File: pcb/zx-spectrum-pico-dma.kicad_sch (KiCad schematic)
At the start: 1 part, among them U101 RP2350_Stamp_XL

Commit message: pull in board from zx diagnostics project
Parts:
- added Z101: ZX48Bus, zxedge:Spectrum_Edge_Connector, symbol zxbus:ZX48Bus
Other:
- moved on the sheet: U101A, U101B
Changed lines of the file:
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@@
 	(symbol
 		(lib_id "rp2350:RP2350_Stamp_XL")
-		(at 83.82 85.09 0)
+		(at 180.34 90.17 0)
 		(unit 1)
 		(exclude_from_sim no)
@@
 		(fields_autoplaced yes)
 		(property "Reference" "U101"
-			(at 83.82 38.1 0)
+			(at 180.34 43.18 0)
 			(effects
 				(font
@@
 		)
 		(property "Value" "RP2350_Stamp_XL"
-			(at 83.82 40.64 0)
+			(at 180.34 45.72 0)
 			(effects
 				(font
@@
 		)
 		(property "Footprint" "rp2350:RP2xxx_Stamp_XL_THT"
-			(at 83.82 85.09 0)
+			(at 180.34 90.17 0)
 			(effects
 				(font
@@
 		)
 		(property "Datasheet" ""
-			(at 83.82 85.09 0)
+			(at 180.34 90.17 0)
 			(effects
 				(font
@@
 		)
 		(property "Description" ""
-			(at 83.82 85.09 0)
+			(at 180.34 90.17 0)
 			(effects
 				(font
@@
 	(symbol
 		(lib_id "rp2350:RP2350_Stamp_XL")
-		(at 143.51 87.63 0)
+		(at 240.03 92.71 0)
 		(unit 2)
 		(exclude_from_sim no)
@@
 		(fields_autoplaced yes)
 		(property "Reference" "U101"
-			(at 143.51 55.88 0)
+			(at 240.03 60.96 0)
 			(effects
 				(font
@@
 		)
 		(property "Value" "RP2350_Stamp_XL"
-			(at 143.51 58.42 0)
+			(at 240.03 63.5 0)
 			(effects
 				(font
@@
 		)
 		(property "Footprint" "rp2350:RP2xxx_Stamp_XL_THT"
-			(at 143.51 87.63 0)
+			(at 240.03 92.71 0)
 			(effects
 				(font
@@
 		)
 		(property "Datasheet" ""
-			(at 143.51 87.63 0)
+			(at 240.03 92.71 0)
 			(effects
 				(font
@@
 		)
 		(property "Description" ""
-			(at 143.51 87.63 0)
+			(at 240.03 92.71 0)
 			(effects
 				(font
@@
 				)
 			)
+		)
+	)
+	(symbol
+		(lib_id "zxbus:ZX48Bus")
+		(at 35.56 125.73 0)
+		(unit 1)
+		(exclude_from_sim no)
+		(in_bom yes)
+		(on_board yes)
+		(dnp no)
+		(fields_autoplaced yes)
+		(property "Reference" "Z101"
+			(at 44.45 38.1 0)
+			(effects
+				(font
+					(size 0.9906 0.9906)
+				)
+			)
+		)
+		(property "Value" "ZX48Bus"
+			(at 44.45 40.64 0)
+			(effects
+				(font
+					(size 0.9906 0.9906)
+				)
+			)
+		)
+		(property "Footprint" "zxedge:Spectrum_Edge_Connector"
+			(at 35.56 125.73 0)
+			(effects
+				(font
+					(size 0.9906 0.9906)
+				)
+				(hide yes)
+			)
+		)
+		(property "Datasheet" ""
+			(at 35.56 125.73 0)
+			(effects
+				(font
+					(size 0.9906 0.9906)
+				)
+				(hide yes)
+			)
+		)
+		(property "Description" ""
+			(at 35.56 125.73 0)
+			(effects
+				(font
+					(size 1.27 1.27)
+				)
+				(hide yes)
+			)
+		)
+		(pin "B8"
+		)
+		(pin "A2"
+		)
+		(pin "B16"
+		)
+		(pin "B15"
+		)
+		(pin "A9"
+		)
+		(pin "A21"
+		)
+		(pin "A20"
+		)
+		(pin "A4"
+		)
+		(pin "B28"
+		)
+		(pin "A25"
+		)
+		(pin "A7"
+		)
+		(pin "B18"
+		)
+		(pin "B6"
+		)
+		(pin "A12"
+		)
+		(pin "B3"
+		)
+		(pin "B4"
+		)
+		(pin "B20"
+		)
+		(pin "B14"
+		)
+		(pin "B9"
+		)
+		(pin "B19"
+		)
+		(pin "B11"
+		)
+		(pin "A22"
+		)
+		(pin "B7"
+		)
+		(pin "A27"
+		)
+		(pin "B10"
+		)
+		(pin "A24"
+		)
+		(pin "A8"
+		)
+		(pin "B17"
+		)
+		(pin "A13"
+		)
+		(pin "B27"
+		)
+		(pin "B12"
+		)
+		(pin "B25"
+		)
+		(pin "B21"
+		)
+		(pin "A6"
+		)
+		(pin "A3"
+		)
+		(pin "A14"
+		)
+		(pin "B1"
+		)
+		(pin "A26"
+		)
+		(pin "A16"
+		)
+		(pin "B13"
+		)
+		(pin "A17"
+		)
+		(pin "A23"
+		)
+		(pin "A18"
+		)
+		(pin "A28"
+		)
+		(pin "A15"
+		)
+		(pin "B23"
+		)
+		(pin "A10"
+		)
+		(pin "A19"
+		)
+		(pin "A11"
+		)
+		(pin "A1"
+		)
+		(pin "B2"
+		)
+		(pin "B24"
+		)
+		(pin "B22"
+		)
+		(pin "B26"
+		)
+		(instances
+			(project ""
+				(path "/d8e2427c-cc3d-4679-b4b6-2ba21d9ca0ef"
+					(reference "Z101")
+					(unit 1)
+				)
+			)

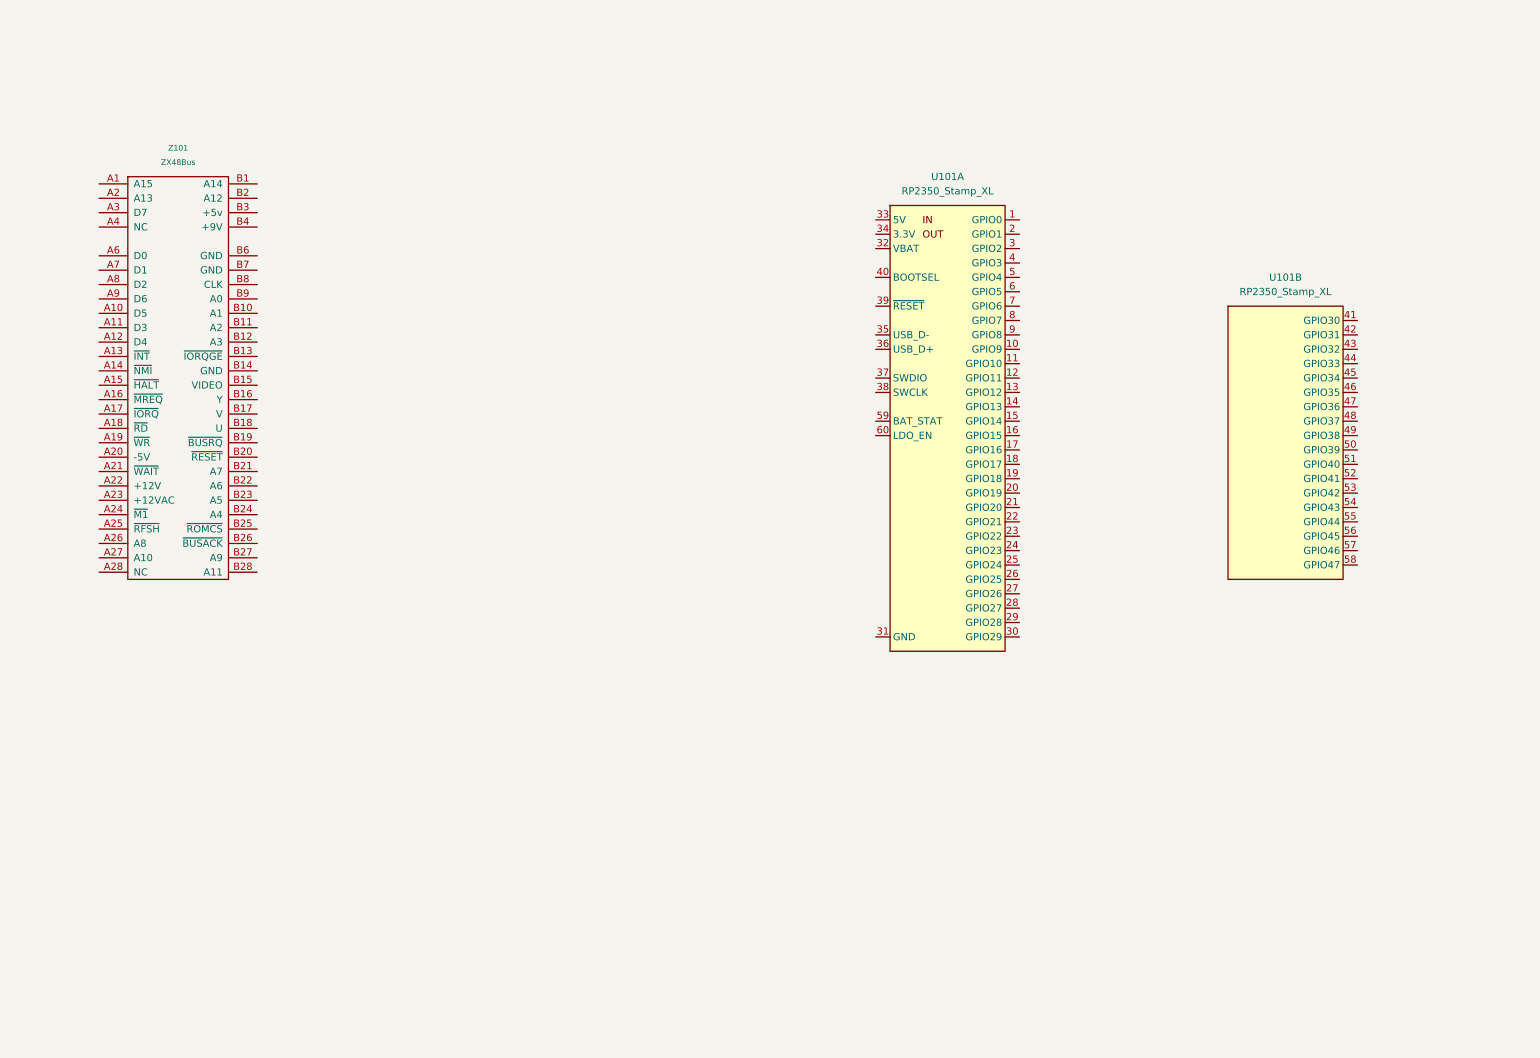
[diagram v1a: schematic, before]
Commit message: flesh out initial schematic
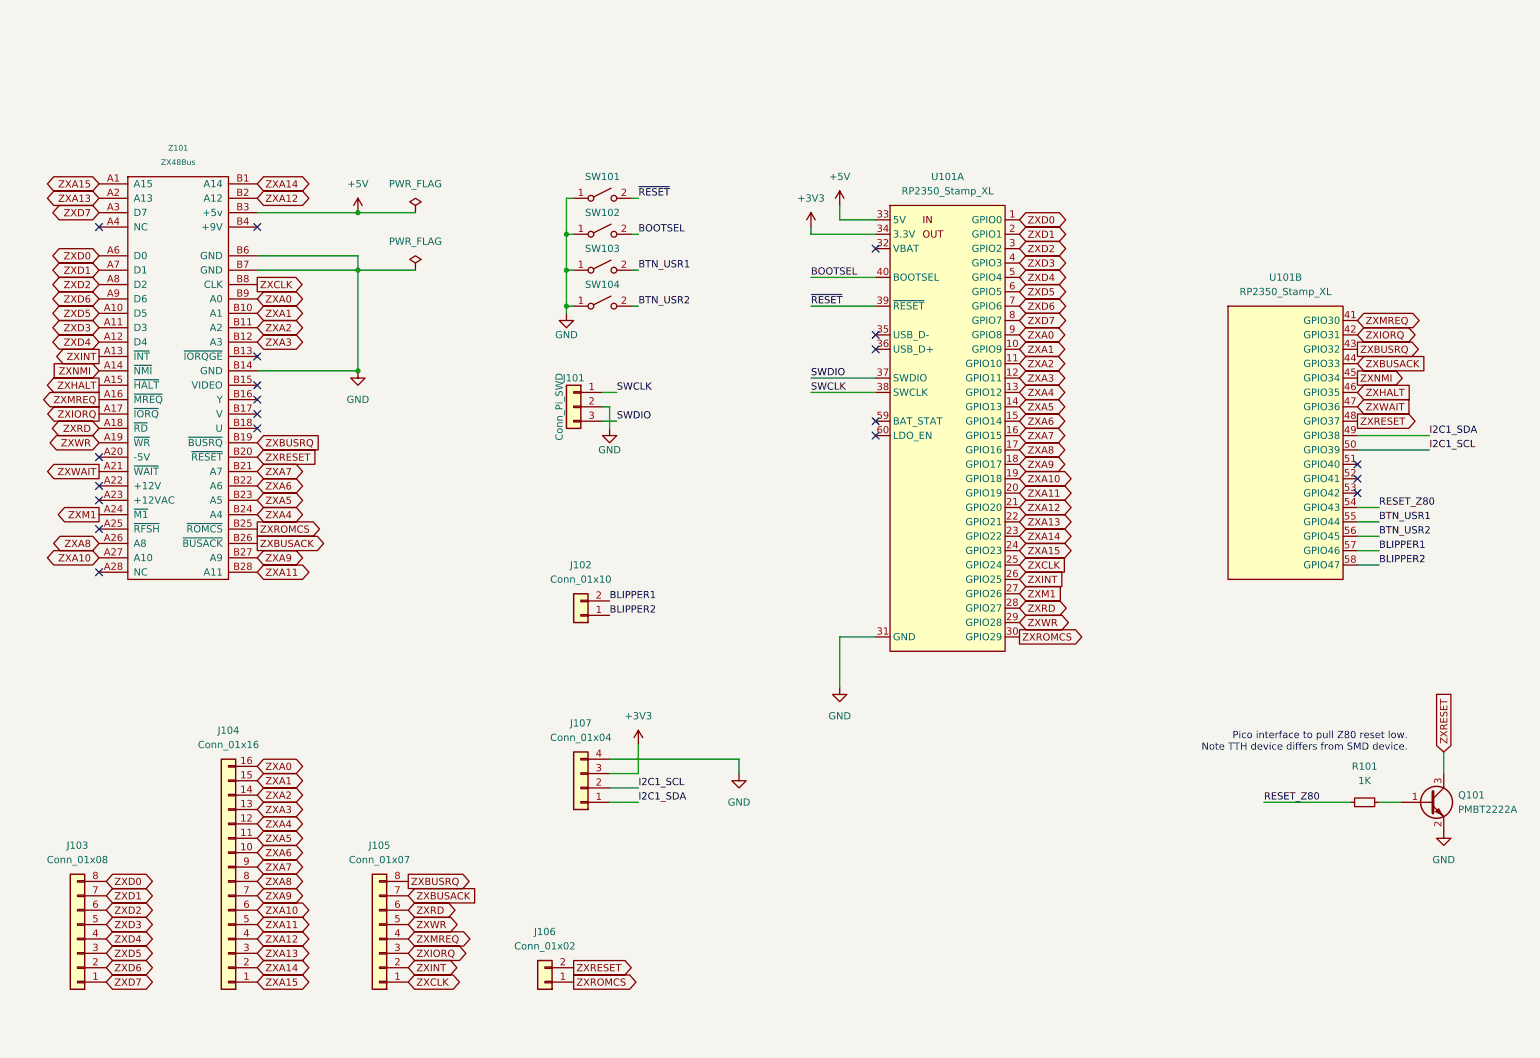
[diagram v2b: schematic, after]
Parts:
- added J101: Conn_Pi_SWD, Connector_PinHeader_2.54mm:PinHeader_1x03_P2.54mm_Vertical, symbol Connector_Generic:Conn_01x03
- added J102: Conn_01x10, symbol Connector_Generic:Conn_01x02
- added J103: Conn_01x08, symbol Connector_Generic:Conn_01x08
- added J104: Conn_01x16, symbol Connector_Generic:Conn_01x16
- added J105: Conn_01x07, symbol Connector_Generic:Conn_01x08
- added J106: Conn_01x02, symbol Connector_Generic:Conn_01x02
- added J107: Conn_01x04, symbol Connector_Generic:Conn_01x04
- added Q101: PMBT2222A, Package_TO_SOT_SMD:TSOT-23_HandSoldering, symbol pmbt2222a:PMBT2222A
- added R101: 1K, Resistor_SMD:R_1206_3216Metric_Pad1.30x1.75mm_HandSolder, symbol Device:R_Small
- added SW101: BTN_RESET, Button_Switch_THT:SW_PUSH_6mm_H4.3mm, symbol Switch:SW_SPST
- added SW102: BTN_BOOTSEL, Button_Switch_THT:SW_PUSH_6mm_H4.3mm, symbol Switch:SW_SPST
- added SW103: BTN_USR1, Button_Switch_THT:SW_PUSH_6mm_H4.3mm, symbol Switch:SW_SPST
- added SW104: BTN_USR2, Button_Switch_THT:SW_PUSH_6mm_H4.3mm, symbol Switch:SW_SPST
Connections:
- net ZXD0: now reaches U101.1 (GPIO0)
- net ZXD0: now also Z101.A6 (D0), J103.8 (Pin_8)
- net ZXA1: now reaches U101.10 (GPIO9)
- net ZXA1: now also Z101.B10 (A1), J104.15 (Pin_15)
- net ZXA2: now reaches U101.11 (GPIO10)
- net ZXA2: now also Z101.B11 (A2), J104.14 (Pin_14)
- net ZXA3: now reaches U101.12 (GPIO11)
- net ZXA3: now also Z101.B12 (A3), J104.13 (Pin_13)
- net ZXA4: now reaches U101.13 (GPIO12)
- net ZXA4: now also Z101.B24 (A4), J104.12 (Pin_12)
- net ZXA5: now reaches U101.14 (GPIO13)
- net ZXA5: now also Z101.B23 (A5), J104.11 (Pin_11)
- net ZXA6: now reaches U101.15 (GPIO14)
- net ZXA6: now also Z101.B22 (A6), J104.10 (Pin_10)
- net ZXA7: now reaches U101.16 (GPIO15)
- net ZXA7: now also Z101.B21 (A7), J104.9 (Pin_9)
- net ZXA8: now reaches U101.17 (GPIO16)
- net ZXA8: now also Z101.A26 (A8), J104.8 (Pin_8)
- net ZXA9: now reaches U101.18 (GPIO17)
- net ZXA9: now also Z101.B27 (A9), J104.7 (Pin_7)
- net ZXA10: now reaches U101.19 (GPIO18)
- net ZXA10: now also Z101.A27 (A10), J104.6 (Pin_6)
- net ZXD1: now reaches U101.2 (GPIO1)
- net ZXD1: now also Z101.A7 (D1), J103.7 (Pin_7)
- net ZXA11: now reaches U101.20 (GPIO19)
- net ZXA11: now also Z101.B28 (A11), J104.5 (Pin_5)
- net ZXA12: now reaches U101.21 (GPIO20)
- net ZXA12: now also Z101.B2 (A12), J104.4 (Pin_4)
- net ZXA13: now reaches U101.22 (GPIO21)
- net ZXA13: now also Z101.A2 (A13), J104.3 (Pin_3)
- net ZXA14: now reaches U101.23 (GPIO22)
- net ZXA14: now also Z101.B1 (A14), J104.2 (Pin_2)
- net ZXA15: now reaches U101.24 (GPIO23)
- net ZXA15: now also Z101.A1 (A15), J104.1 (Pin_1)
- net ZXCLK: now reaches U101.25 (GPIO24)
- net ZXCLK: now also Z101.B8 (CLK), J105.1 (Pin_1)
- net ZXINT: now reaches U101.26 (GPIO25)
- net ZXINT: now also Z101.A13 (~{INT}), J105.2 (Pin_2)
- net ZXM1: now reaches U101.27 (GPIO26)
- net ZXM1: now also Z101.A24 (~{M1})
- net ZXRD: now reaches U101.28 (GPIO27)
- net ZXRD: now also Z101.A18 (~{RD}), J105.6 (Pin_6)
- net ZXWR: now reaches U101.29 (GPIO28)
- net ZXWR: now also Z101.A19 (~{WR}), J105.5 (Pin_5)
- net ZXD2: now reaches U101.3 (GPIO2)
- net ZXD2: now also Z101.A8 (D2), J103.6 (Pin_6)
- net ZXROMCS: now reaches U101.30 (GPIO29)
- net ZXROMCS: now also Z101.B25 (~{ROMCS}), J106.1 (Pin_1)
- net GND: now reaches U101.31 (GND)
- net GND: now also Z101.B14 (GND), Z101.B6 (GND), Z101.B7 (GND), J101.2 (Pin_2), J107.4 (Pin_4), Q101.2 (E), SW101.1 (A), SW102.1 (A), SW103.1 (A), SW104.1 (A)
- net +5V: now reaches U101.33 (5V)
- net +5V: now also Z101.B3 (+5v)
- net +3V3: now reaches U101.34 (3.3V)
- net +3V3: now also J107.3 (Pin_3)
- net SWDIO: now reaches U101.37 (SWDIO)
- net SWDIO: now also J101.3 (Pin_3)
- net SWCLK: now reaches U101.38 (SWCLK)
- net SWCLK: now also J101.1 (Pin_1)
- net ~{RESET}: now reaches U101.39 (~{RESET})
- net ~{RESET}: now also SW101.2 (B)
- net ZXD3: now reaches U101.4 (GPIO3)
- net ZXD3: now also Z101.A11 (D3), J103.5 (Pin_5)
- net BOOTSEL: now reaches U101.40 (BOOTSEL)
- net BOOTSEL: now also SW102.2 (B)
- net ZXD4: now reaches U101.5 (GPIO4)
- net ZXD4: now also Z101.A12 (D4), J103.4 (Pin_4)
- net ZXD5: now reaches U101.6 (GPIO5)
- net ZXD5: now also Z101.A10 (D5), J103.3 (Pin_3)
- net ZXD6: now reaches U101.7 (GPIO6)
- net ZXD6: now also Z101.A9 (D6), J103.2 (Pin_2)
- net ZXD7: now reaches U101.8 (GPIO7)
- net ZXD7: now also Z101.A3 (D7), J103.1 (Pin_1)
- net ZXA0: now reaches U101.9 (GPIO8)
- net ZXA0: now also Z101.B9 (A0), J104.16 (Pin_16)
- net ZXMREQ: now reaches U101.41 (GPIO30)
- net ZXMREQ: now also Z101.A16 (~{MREQ}), J105.4 (Pin_4)
- net ZXIORQ: now reaches U101.42 (GPIO31)
- net ZXIORQ: now also Z101.A17 (~{IORQ}), J105.3 (Pin_3)
- net ZXBUSRQ: now reaches U101.43 (GPIO32)
- net ZXBUSRQ: now also Z101.B19 (~{BUSRQ}), J105.8 (Pin_8)
- net ZXBUSACK: now reaches U101.44 (GPIO33)
- net ZXBUSACK: now also Z101.B26 (~{BUSACK}), J105.7 (Pin_7)
- net ZXNMI: now reaches U101.45 (GPIO34)
- net ZXNMI: now also Z101.A14 (~{NMI})
- net ZXHALT: now reaches U101.46 (GPIO35)
- net ZXHALT: now also Z101.A15 (~{HALT})
- net ZXWAIT: now reaches U101.47 (GPIO36)
- net ZXWAIT: now also Z101.A21 (~{WAIT})
- net ZXRESET: now reaches U101.48 (GPIO37)
- net ZXRESET: now also Z101.B20 (~{RESET}), J106.2 (Pin_2), Q101.3 (C)
- net I2C1_SDA: now reaches U101.49 (GPIO38)
- net I2C1_SDA: now also J107.1 (Pin_1)
- net I2C1_SCL: now reaches U101.50 (GPIO39)
- net I2C1_SCL: now also J107.2 (Pin_2)
- net RESET_Z80: now reaches U101.54 (GPIO43)
- net RESET_Z80: now also R101.1
- net BTN_USR1: now reaches U101.55 (GPIO44)
- net BTN_USR1: now also SW103.2 (B)
- net BTN_USR2: now reaches U101.56 (GPIO45)
- net BTN_USR2: now also SW104.2 (B)
- net BLIPPER1: now reaches U101.57 (GPIO46)
- net BLIPPER1: now also J102.2 (Pin_2)
- net BLIPPER2: now reaches U101.58 (GPIO47)
- net BLIPPER2: now also J102.1 (Pin_1)
- new net: Q101.1 (B), R101.2
- no-connect marks 0 -> 20
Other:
- note added: "Pico interface to pull Z80 reset low. Note TTH device differs from SMD device."

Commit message: more layout work
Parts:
- added H101: +5V, MountingHole:MountingHole_2.2mm_M2_Pad, symbol Mechanical:MountingHole_Pad
- added H102: +3V3, MountingHole:MountingHole_2.2mm_M2_Pad, symbol Mechanical:MountingHole_Pad
- added H103: GND, MountingHole:MountingHole_2.2mm_M2_Pad, symbol Mechanical:MountingHole_Pad
- added J108: Spare GPIOs, Connector_PinHeader_2.54mm:PinHeader_1x03_P2.54mm_Vertical, symbol Connector_Generic:Conn_01x03
- J101: value Conn_Pi_SWD -> SWD
- J102: value Conn_01x10 -> Blippers; footprint (none) -> Connector_PinHeader_2.54mm:PinHeader_1x02_P2.54mm_Vertical
- J103: value Conn_01x08 -> Z80 Data Bus; footprint (none) -> Connector_PinHeader_2.54mm:PinHeader_1x08_P2.54mm_Vertical
- J104: value Conn_01x16 -> Z80 Address Bus; footprint (none) -> Connector_PinHeader_2.54mm:PinHeader_1x16_P2.54mm_Vertical
- J105: value Conn_01x07 -> Z80 Control Bus; footprint (none) -> Connector_PinHeader_2.54mm:PinHeader_1x08_P2.54mm_Vertical
- J106: value Conn_01x02 -> ZX Control; footprint (none) -> Connector_PinHeader_2.54mm:PinHeader_1x02_P2.54mm_Vertical
- J107: value Conn_01x04 -> OLED; footprint (none) -> Connector_PinHeader_2.54mm:PinHeader_1x04_P2.54mm_Vertical
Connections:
- net +3V3: now also H102.1
- net +5V: now also H101.1
- net GND: now also H103.1
- net GPIO40: now reaches U101.51 (GPIO40)
- net GPIO40: now also J108.3 (Pin_3)
- net GPIO41: now reaches U101.52 (GPIO41)
- net GPIO41: now also J108.2 (Pin_2)
- net GPIO42: now reaches U101.53 (GPIO42)
- net GPIO42: now also J108.1 (Pin_1)
- no-connect marks 20 -> 17
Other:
- note added: "Input buttons"
- note added: "Interface to pull Z80 reset low. Note TTH device differs from SMD device."
- note added: "OLED Screen"
- note added: "SWD programming"
- note added: "Scope blippers"
- note added: "Spare GPIOs"
- note added: "Spectrum/Z80 signals"
- note removed: "Pico interface to pull Z80 reset low. Note TTH device differs from SMD device."
- title: (none) -> RP2350B Spectrum DMA Interface
- moved on the sheet: J101, J106, Q101, R101, SW101, SW102, SW103, SW104, U101A, U101B
